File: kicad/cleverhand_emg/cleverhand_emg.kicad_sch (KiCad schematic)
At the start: 21 parts, among them J1 COM_IN, J2 COM_OUT, U1 MCP3564RT-ENC, U2 SN74LVC86ARGYR, U4 SN74ALVC08RGYR, U5 SN74LVC1G132DCKR

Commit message: finished v3
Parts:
- added C3: 10uF, Capacitor_SMD:C_0402_1005Metric, symbol Device:C
- JP1: value SolderJumper_3_Bridged12 -> 1-4_neo_bridge; footprint (none) -> Jumper:SolderJumper-3_P1.3mm_Bridged12_RoundedPad1.0x1.5mm_NumberLabels
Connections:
- net CH_REF: now also U1.1 (REFIN-)
- net GNDA: now also C3.2
- net NEO_OUT: now also JP1.3 (B)
- net at D2.1 (DIN): now also JP1.1 (A); no longer D1.3 (DOUT)
- net at U1.2 (REFIN+/OUT): now also C3.1
- net at JP1.2 (C): now also D1.3 (DOUT)
- no-connect marks 0 -> 15
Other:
- moved on the sheet: D1

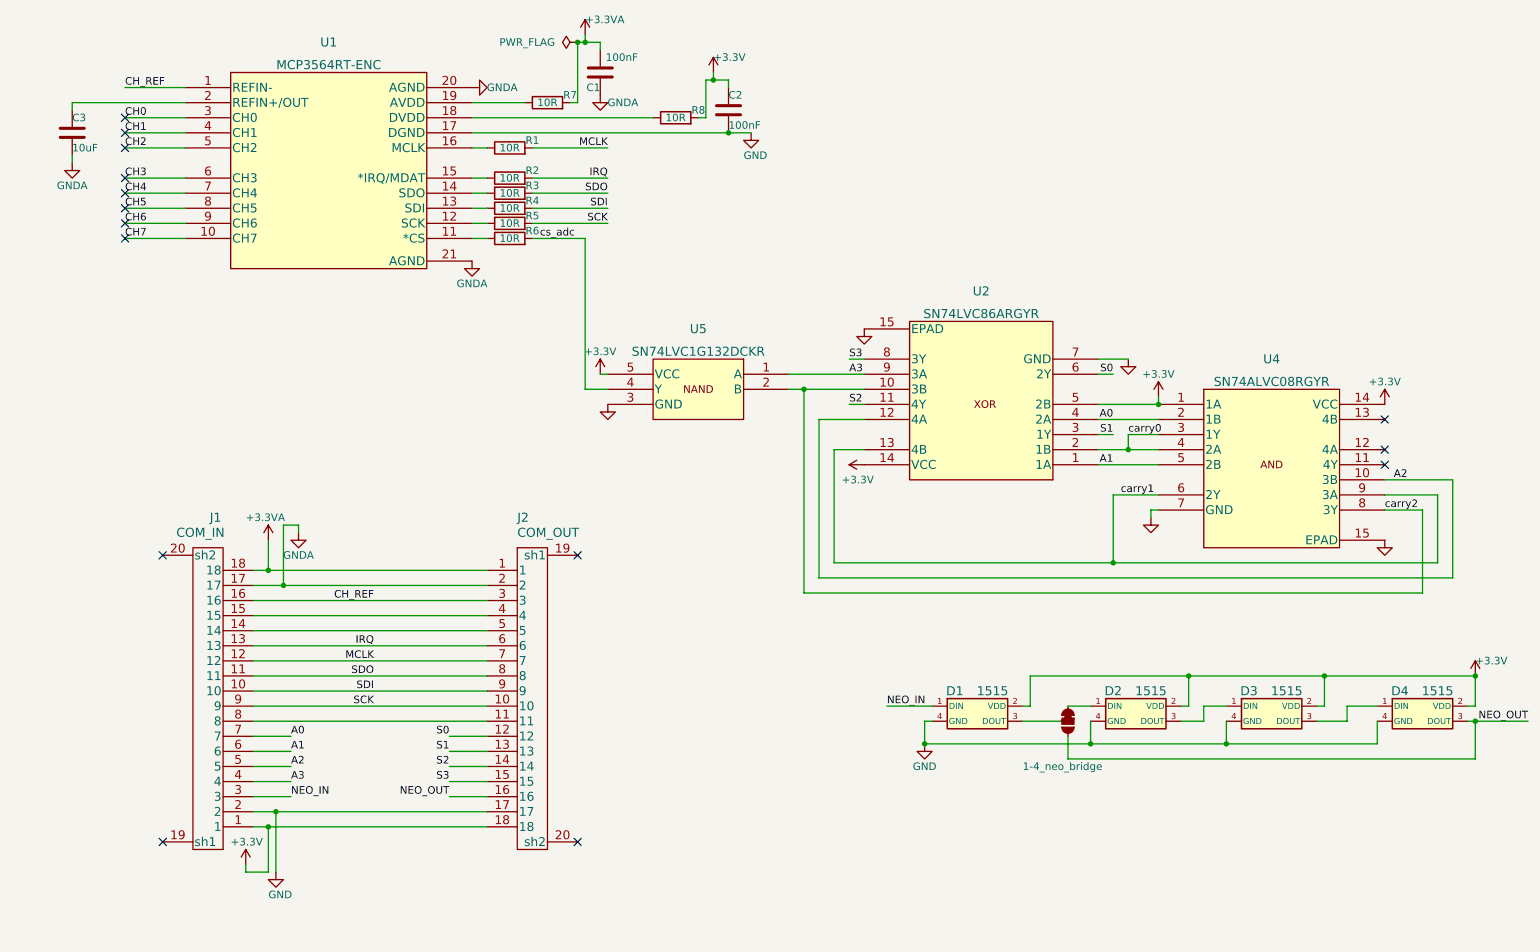
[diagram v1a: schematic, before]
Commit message: fixed some panel bug for jlcpcb
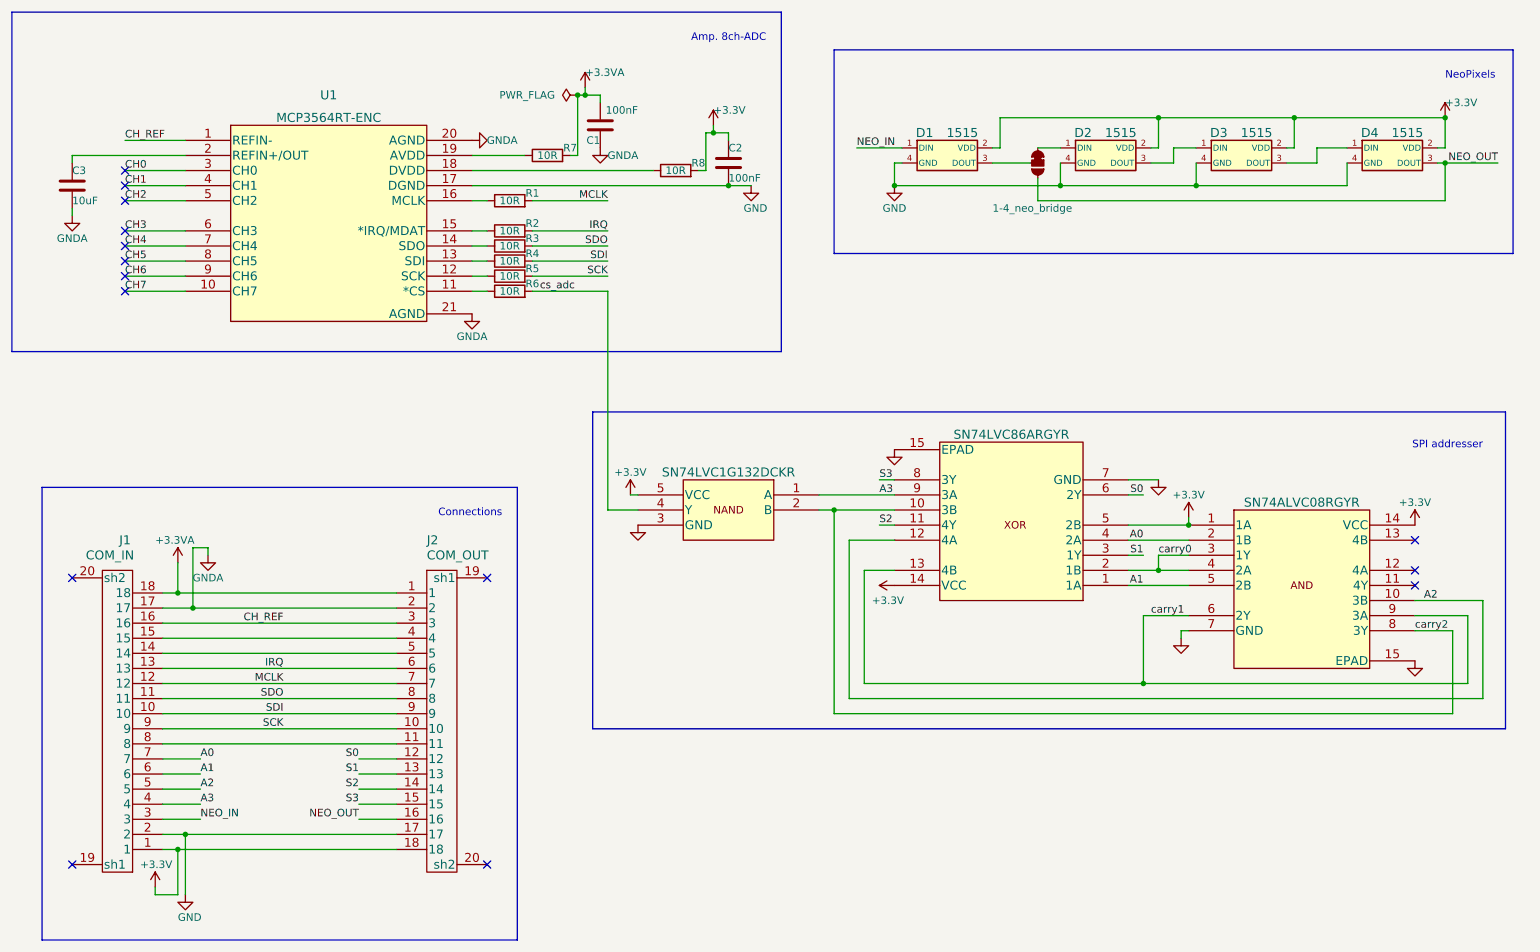
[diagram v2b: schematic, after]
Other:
- note added: "Amp. 8ch-ADC"
- note added: "Connections"
- note added: "NeoPixels"
- note added: "SPI addresser"
- moved on the sheet: C1, C2, C3, D1, D2, D3, D4, J1, J2, R1, R2, R3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

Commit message: v3.1 fixed solder and paste mask and some via pos
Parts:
- added TP1, TP2, TP4: TestPoint_Probe, TestPoint:TestPoint_Pad_D1.0mm, symbol Connector:TestPoint_Probe
- added TP3: TestPoint_Probe, symbol Connector:TestPoint_Probe
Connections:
- net cs_adc: now also TP4.1
- net AUX2: now reaches J1.14, J2.5
- net AUX2: now also TP2.1
- net AUX3: now reaches J1.15, J2.4
- net AUX3: now also TP3.1
- net AUX1: now reaches J1.8, J2.11
- net AUX1: now also TP1.1
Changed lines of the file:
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@@
   (junction (at 162.56 116.84) (diameter 0) (color 0 0 0 0)
   )
+  (junction (at 72.39 156.21) (diameter 0) (color 0 0 0 0)
+  )
+  (junction (at 124.46 96.52) (diameter 0) (color 0 0 0 0)
+  )
   (junction (at 53.34 171.45) (diameter 0) (color 0 0 0 0)
   )
@@
   (junction (at 265.43 50.8) (diameter 0) (color 0 0 0 0)
   )
+  (junction (at 72.39 138.43) (diameter 0) (color 0 0 0 0)
+  )
   (junction (at 52.07 130.81) (diameter 0) (color 0 0 0 0)
   )
@@
   )
   (junction (at 120.65 46.99) (diameter 0) (color 0 0 0 0)
+  )
+  (junction (at 74.93 140.97) (diameter 0) (color 0 0 0 0)
   )
   (junction (at 240.03 50.8) (diameter 0) (color 0 0 0 0)
@@
     (stroke (width 0) (type default) (color 0 0 0 0))
   )
+  (wire (pts (xy 72.39 138.43) (xy 49.53 138.43))
+    (stroke (width 0) (type default) (color 0 0 0 0))
+  )
   (wire (pts (xy 34.29 67.31) (xy 34.29 66.04))
     (stroke (width 0) (type default) (color 0 0 0 0))
@@
     (stroke (width 0) (type default) (color 0 0 0 0))
   )
+  (wire (pts (xy 72.39 138.43) (xy 88.9 138.43))
+    (stroke (width 0) (type default) (color 0 0 0 0))
+  )
   (wire (pts (xy 55.88 168.91) (xy 49.53 168.91))
     (stroke (width 0) (type default) (color 0 0 0 0))
@@
     (stroke (width 0) (type default) (color 0 0 0 0))
   )
+  (wire (pts (xy 74.93 140.97) (xy 49.53 140.97))
+    (stroke (width 0) (type default) (color 0 0 0 0))
+  )
   (wire (pts (xy 142.24 52.07) (xy 142.24 53.34))
     (stroke (width 0) (type default) (color 0 0 0 0))
@@
     (stroke (width 0) (type default) (color 0 0 0 0))
   )
+  (wire (pts (xy 49.53 156.21) (xy 72.39 156.21))
+    (stroke (width 0) (type default) (color 0 0 0 0))
+  )
   (wire (pts (xy 212.09 127) (xy 217.17 127))
     (stroke (width 0) (type default) (color 0 0 0 0))
@@
     (stroke (width 0) (type default) (color 0 0 0 0))
   )
+  (wire (pts (xy 124.46 96.52) (xy 124.46 116.84))
+    (stroke (width 0) (type default) (color 0 0 0 0))
+  )
   (polyline (pts (xy 162.56 39.37) (xy 162.56 73.66))
     (stroke (width 0) (type default) (color 0 0 0 0))
@@
     (stroke (width 0) (type default) (color 0 0 0 0))
   )
-  (wire (pts (xy 88.9 140.97) (xy 49.53 140.97))
-    (stroke (width 0) (type default) (color 0 0 0 0))
-  )
   (wire (pts (xy 140.97 53.34) (xy 140.97 59.69))
     (stroke (width 0) (type default) (color 0 0 0 0))
@@
     (stroke (width 0) (type default) (color 0 0 0 0))
   )
+  (wire (pts (xy 74.93 140.97) (xy 88.9 140.97))
+    (stroke (width 0) (type default) (color 0 0 0 0))
+  )
   (wire (pts (xy 220.98 137.16) (xy 220.98 138.43))
     (stroke (width 0) (type default) (color 0 0 0 0))
@@
     (stroke (width 0) (type default) (color 0 0 0 0))
   )
-  (wire (pts (xy 88.9 138.43) (xy 49.53 138.43))
-    (stroke (width 0) (type default) (color 0 0 0 0))
-  )
   (wire (pts (xy 162.56 116.84) (xy 172.72 116.84))
     (stroke (width 0) (type default) (color 0 0 0 0))
   )
-  (wire (pts (xy 124.46 80.01) (xy 124.46 116.84))
+  (wire (pts (xy 124.46 80.01) (xy 124.46 96.52))
     (stroke (width 0) (type default) (color 0 0 0 0))
   )
@@
     (stroke (width 0) (type default) (color 0 0 0 0))
   )
-  (wire (pts (xy 88.9 156.21) (xy 49.53 156.21))
+  (wire (pts (xy 88.9 156.21) (xy 72.39 156.21))
     (stroke (width 0) (type default) (color 0 0 0 0))
   )
@@
     (effects (font (size 1.27 1.27)) (justify left bottom))
   )
+  (label "AUX2" (at 69.85 140.97 180)
+    (effects (font (size 1.27 1.27)) (justify right bottom))
+  )
   (label "A2" (at 55.88 163.83 0)
     (effects (font (size 1.27 1.27)) (justify left bottom))
@@
     (effects (font (size 1.27 1.27)) (justify right bottom))
   )
+  (label "AUX1" (at 69.85 156.21 180)
+    (effects (font (size 1.27 1.27)) (justify right bottom))
+  )
   (label "SDO" (at 124.46 72.39 180)
     (effects (font (size 1.27 1.27)) (justify right bottom))
@@
     (effects (font (size 1.27 1.27)) (justify right bottom))
   )
+  (label "AUX3" (at 69.85 138.43 180)
+    (effects (font (size 1.27 1.27)) (justify right bottom))
+  )
   (label "A2" (at 264.16 132.08 180)
     (effects (font (size 1.27 1.27)) (justify right bottom))
@@
   (label "S1" (at 214.63 124.46 180)
     (effects (font (size 1.27 1.27)) (justify right bottom))
+  )
+  (symbol (lib_id "Connector:TestPoint_Probe") (at 72.39 138.43 0) (unit 1)
+    (in_bom yes) (on_board yes) (fields_autoplaced)
+    (property "Reference" "TP3" (id 0) (at 76.2 136.8424 0)
+      (effects (font (size 1.27 1.27)) (justify left))
+    )
+    (property "Value" "TestPoint_Probe" (id 1) (at 76.2 138.1124 0)
+      (effects (font (size 1.27 1.27)) (justify left) hide)
+    )
+    (property "Footprint" "" (id 2) (at 77.47 138.43 0)
+      (effects (font (size 1.27 1.27)) hide)
+    )
+    (property "Datasheet" "~" (id 3) (at 77.47 138.43 0)
+      (effects (font (size 1.27 1.27)) hide)
+    )
+    (pin "1")
   )
   (symbol (lib_id "SN74LVC1G132DCKR:SN74LVC1G132DCKR") (at 160.02 114.3 0) (mirror y) (unit 1)
@@
     (pin "1")
   )
+  (symbol (lib_id "Connector:TestPoint_Probe") (at 74.93 140.97 0) (unit 1)
+    (in_bom yes) (on_board yes) (fields_autoplaced)
+    (property "Reference" "TP2" (id 0) (at 78.74 139.3824 0)
+      (effects (font (size 1.27 1.27)) (justify left))
+    )
+    (property "Value" "TestPoint_Probe" (id 1) (at 78.74 140.6524 0)
+      (effects (font (size 1.27 1.27)) (justify left) hide)
+    )
+    (property "Footprint" "TestPoint:TestPoint_Pad_D1.0mm" (id 2) (at 80.01 140.97 0)
+      (effects (font (size 1.27 1.27)) hide)
+    )
+    (property "Datasheet" "~" (id 3) (at 80.01 140.97 0)
+      (effects (font (size 1.27 1.27)) hide)
+    )
+    (pin "1")
+  )
+  (symbol (lib_id "Connector:TestPoint_Probe") (at 124.46 96.52 0) (unit 1)
+    (in_bom yes) (on_board yes) (fields_autoplaced)
+    (property "Reference" "TP4" (id 0) (at 128.27 94.9324 0)
+      (effects (font (size 1.27 1.27)) (justify left))
+    )
+    (property "Value" "TestPoint_Probe" (id 1) (at 128.27 96.2024 0)
+      (effects (font (size 1.27 1.27)) (justify left) hide)
+    )
+    (property "Footprint" "TestPoint:TestPoint_Pad_D1.0mm" (id 2) (at 129.54 96.52 0)
+      (effects (font (size 1.27 1.27)) hide)
+    )
+    (property "Datasheet" "~" (id 3) (at 129.54 96.52 0)
+      (effects (font (size 1.27 1.27)) hide)
+    )
+    (pin "1")
+  )
   (symbol (lib_id "power:PWR_FLAG") (at 119.38 46.99 90) (unit 1)
     (in_bom yes) (on_board yes) (fields_autoplaced)
@@
     (pin "1")
   )
+  (symbol (lib_id "Connector:TestPoint_Probe") (at 72.39 156.21 0) (mirror x) (unit 1)
+    (in_bom yes) (on_board yes)
+    (property "Reference" "TP1" (id 0) (at 74.93 160.02 0)
+      (effects (font (size 1.27 1.27)) (justify right))
+    )
+    (property "Value" "TestPoint_Probe" (id 1) (at 71.12 159.0674 0)
+      (effects (font (size 1.27 1.27)) (justify right) hide)
+    )
+    (property "Footprint" "TestPoint:TestPoint_Pad_D1.0mm" (id 2) (at 77.47 156.21 0)
+      (effects (font (size 1.27 1.27)) hide)
+    )
+    (property "Datasheet" "~" (id 3) (at 77.47 156.21 0)
+      (effects (font (size 1.27 1.27)) hide)
+    )
+    (pin "1")
+  )
   (symbol (lib_id "power:+3.3V") (at 142.24 52.07 0) (unit 1)
     (in_bom yes) (on_board yes)
@@
       (reference "R8") (unit 1) (value "10R") (footprint "Resistor_SMD:R_0402_1005Metric")
     )
+    (path "/ab701824-0bf4-4a6f-8975-f9521fec287d"
+      (reference "TP1") (unit 1) (value "TestPoint_Probe") (footprint "TestPoint:TestPoint_Pad_D1.0mm")
+    )
+    (path "/5aa95592-2f36-4637-8919-aca78b942b8e"
+      (reference "TP2") (unit 1) (value "TestPoint_Probe") (footprint "TestPoint:TestPoint_Pad_D1.0mm")
+    )
+    (path "/08c3a209-1534-4797-ac31-f794ac5a36a6"
+      (reference "TP3") (unit 1) (value "TestPoint_Probe") (footprint "TestPoint:TestPoint_Pad_D1.0mm")
+    )
+    (path "/5cf8b9b9-d3b7-4c66-a12b-7f63d35ffdf0"
+      (reference "TP4") (unit 1) (value "TestPoint_Probe") (footprint "TestPoint:TestPoint_Pad_D1.0mm")
+    )
     (path "/71abaf04-6918-4f74-8990-a50212145c03"
